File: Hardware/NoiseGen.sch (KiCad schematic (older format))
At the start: 42 parts

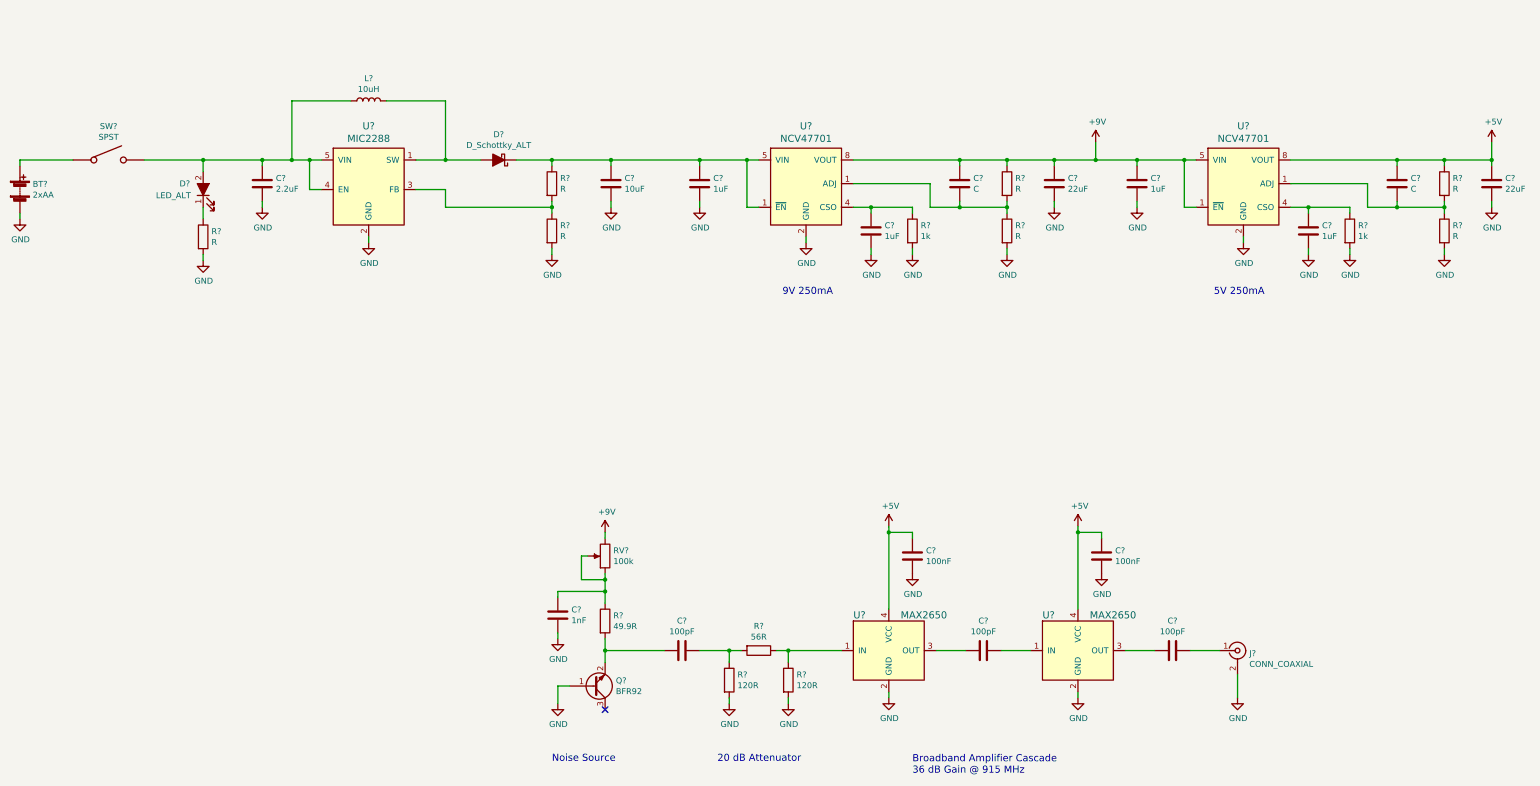
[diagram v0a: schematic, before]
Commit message: Finished schematic & BOM
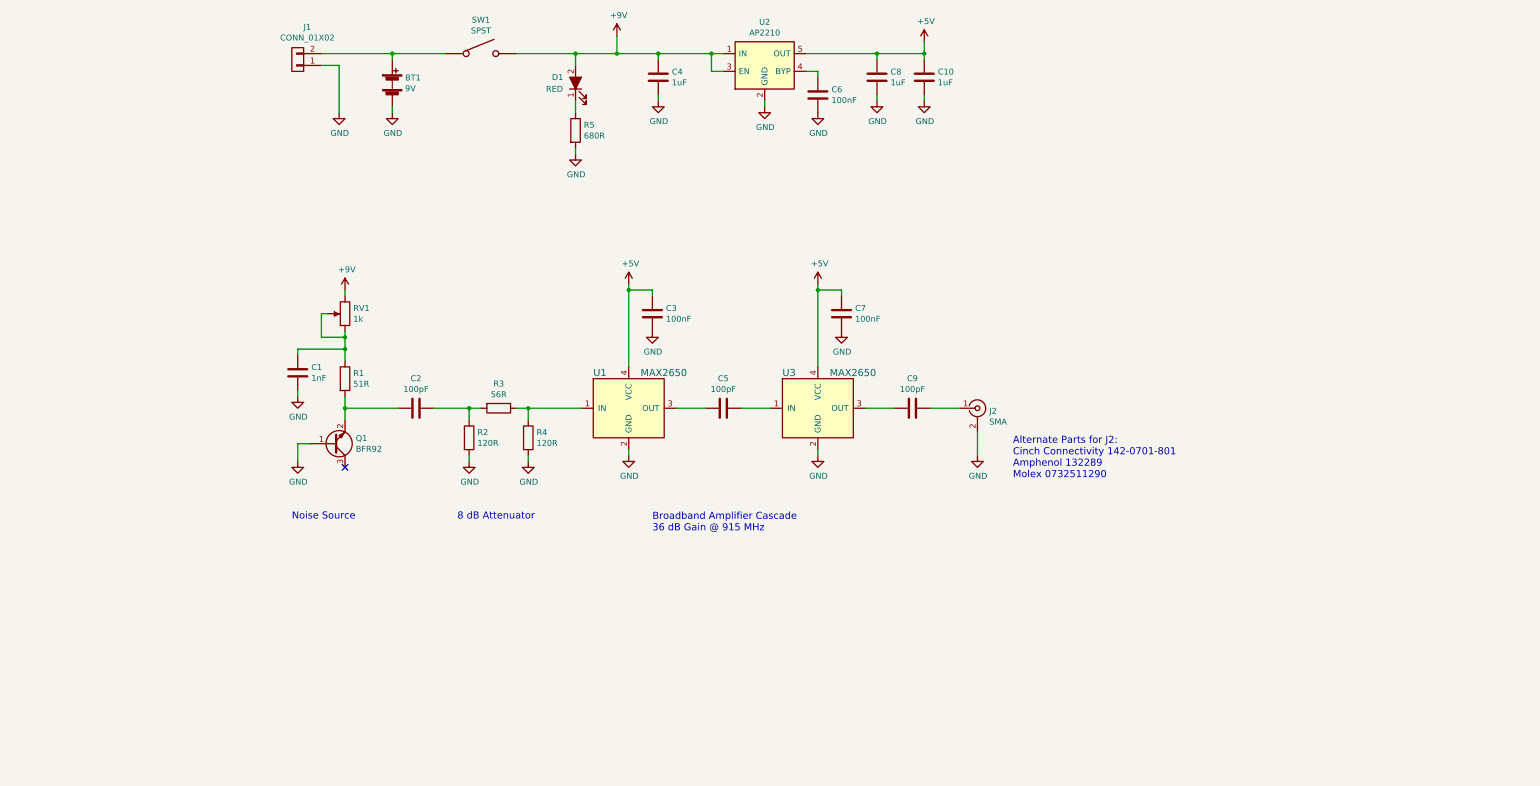
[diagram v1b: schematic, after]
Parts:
- removed C? (x2): C, symbol C
- removed C? (x3): 1uF, symbol C
- removed C? (x2): 22uF, symbol C
- removed C?: 2.2uF, symbol C
- removed C?: 10uF, symbol C
- removed D?: D_Schottky_ALT, symbol D_Schottky_ALT
- removed L?: 10uH, symbol L
- removed R? (x2): 1k, symbol R
- removed R? (x6): R, symbol R
- removed U? (x2): NCV47701, symbol NCV47701
- removed U?: MIC2288, symbol MIC2288
- added C10, C8: 1uF, symbol C
- added C6: 100nF, symbol C
- added J1: CONN_01X02, symbol CONN_01X02
- added U2: AP2210, TO_SOT_Packages_SMD:SOT-23-5, symbol AP2210
- BT1: renamed from BT?; value 2xAA -> 9V
- D1: renamed from D?; value LED_ALT -> RED
- J2: renamed from J?; value CONN_COAXIAL -> SMA
- R1: renamed from R?; value 49.9R -> 51R
- R5: renamed from R?; value R -> 680R
- RV1: renamed from RV?; value 100k -> 1k
- gave numbers to parts that had none: 14
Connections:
- net +5V: now also C10.1, C8.1, U2.5 (OUT)
- net +9V: now also D1.2 (A), SW1.2, U2.1 (IN), U2.3 (EN)
- net GND: now also C10.2, C6.2, C8.2, J1.1 (P1), U2.2 (GND)
- net at BT1.1 (+), SW1.1: now also J1.2 (P2)
- new net: C6.1, U2.4 (BYP)
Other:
- note added: "8 dB Attenuator"
- note added: "Alternate Parts for J2:\nCinch Connectivity 142-0701-801\nAmphenol 132289\nMolex 0732511290"
- note removed: "20 dB Attenuator"
- note removed: "5V 250mA"
- note removed: "9V 250mA"
- moved on the sheet: BT1, C1, C2, C3, C4, C5, C7, C9, D1, J2, Q1, R1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
